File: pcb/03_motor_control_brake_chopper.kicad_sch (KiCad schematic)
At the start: 0 parts

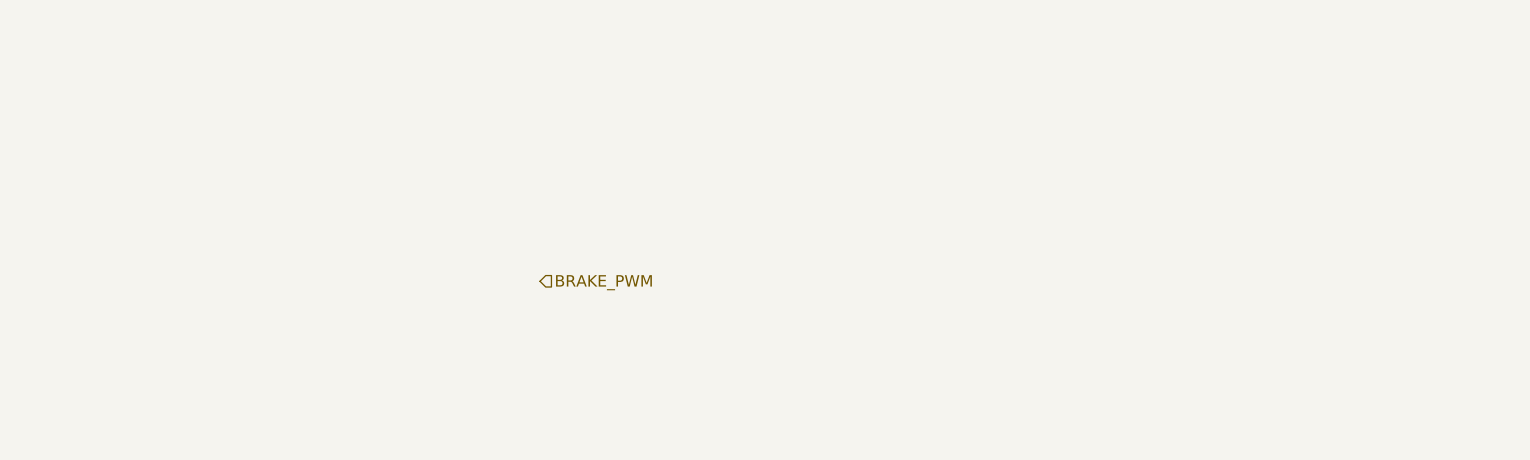
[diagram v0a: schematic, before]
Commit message: Implemented brake chopper control with low side mosfet
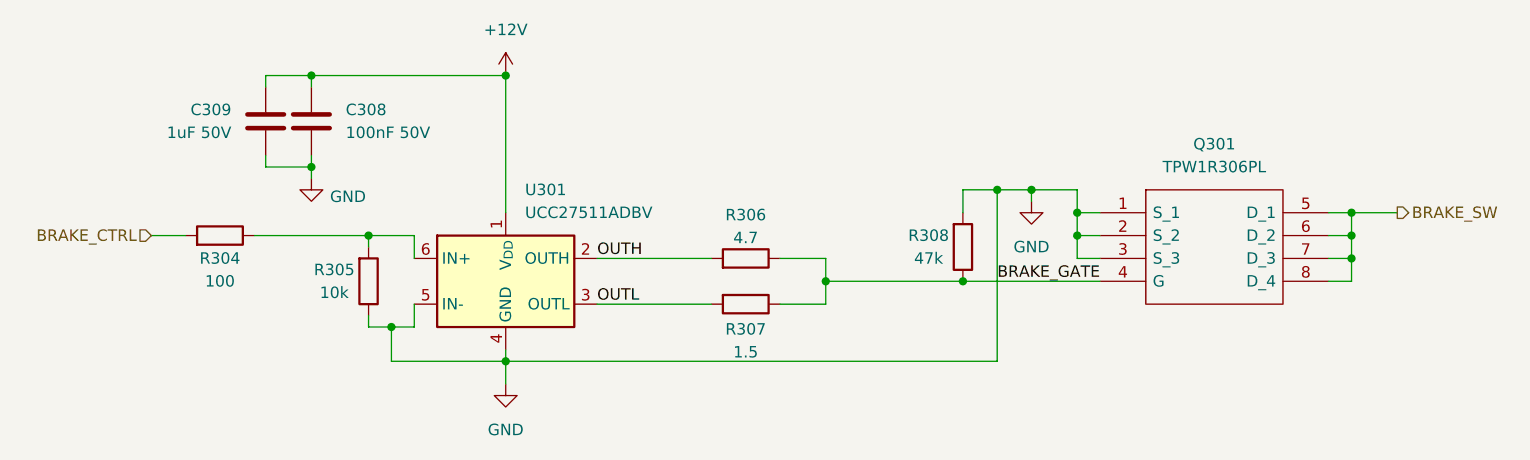
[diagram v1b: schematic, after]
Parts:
- added C308: 100nF 50V, FluxNode-FOC:C_0402_1005_DensityHigh, symbol Device:C
- added C309: 1uF 50V, FluxNode-FOC:C_0603_1608_DensityHigh, symbol Device:C
- added Q301: TPW1R306PL, FluxNode-FOC:SOP_ADVANCE, symbol FluxNode-FOC:TPW1R306PL
- added R304: 100, FluxNode-FOC:R_0402_1005_DensityHigh, symbol Device:R
- added R305: 10k, FluxNode-FOC:R_0402_1005_DensityHigh, symbol Device:R
- added R306: 4.7, FluxNode-FOC:R_0603_1608_DensityHigh, symbol Device:R
- added R307: 1.5, FluxNode-FOC:R_0603_1608_DensityHigh, symbol Device:R
- added R308: 47k, FluxNode-FOC:R_0402_1005_DensityHigh, symbol Device:R
- added U301: UCC27511ADBV, Package_TO_SOT_SMD:SOT-23-6, symbol Driver_FET:UCC27511ADBV
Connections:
- new net: R304.1, R305.2, U301.6 (IN+)
- new net +12V: C308.1, C309.1, U301.1 (V_{DD})
- new net BRAKE_CTRL: R304.2
- new net BRAKE_GATE: Q301.4 (G), R306.1, R307.1, R308.1
- new net BRAKE_SW: Q301.5 (D_1), Q301.6 (D_2), Q301.7 (D_3), Q301.8 (D_4)
- new net GND: C308.2, C309.2, Q301.1 (S_1), Q301.2 (S_2), Q301.3 (S_3), R305.1, R308.2, U301.4 (GND), U301.5 (IN-)
- new net OUTH: R306.2, U301.2 (OUTH)
- new net OUTL: R307.2, U301.3 (OUTL)

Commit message: Unified all different LCSC part numbers of the same exact components to just one variant
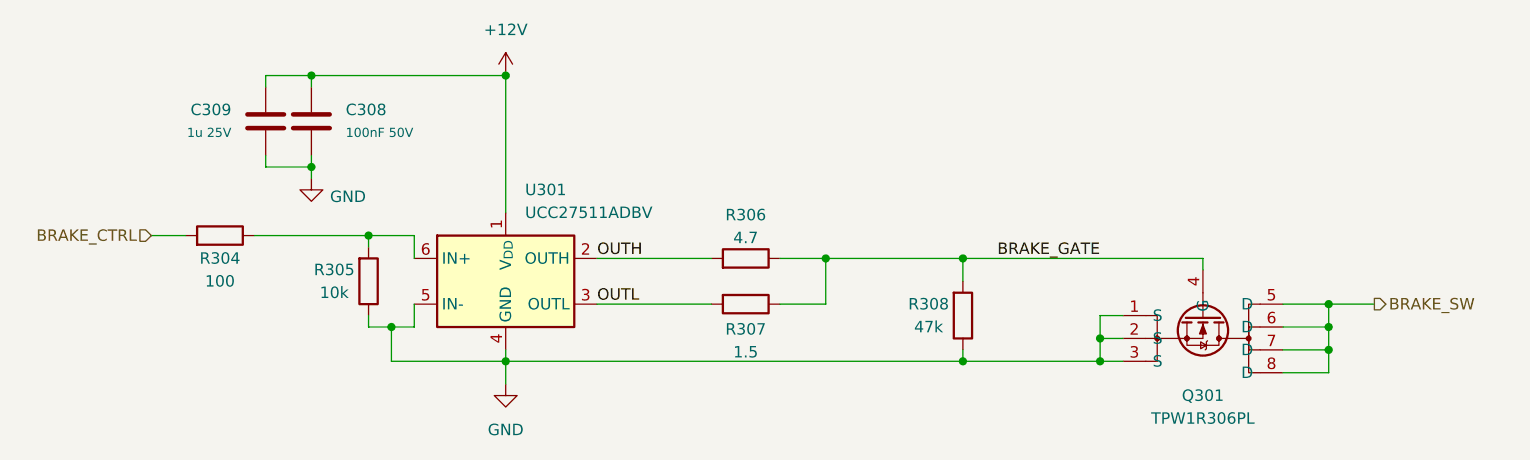
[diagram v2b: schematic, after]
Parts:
- C308: LCSC (none) -> C361198; MPN (none) -> C1005X7R1H104KT000F
- C309: value 1uF 50V -> 1u 25V; LCSC (none) -> C386079; MPN (none) -> TMK107AB7105KAHT
- R304: LCSC (none) -> C705627; MPN (none) -> RT0402BRD07100RL
- R306: LCSC (none) -> C54921054; MPN (none) -> HRC0603J4R7 ENTN
- R307: LCSC (none) -> C2906978; MPN (none) -> FRC0603F1R50TS
- R308: LCSC (none) -> C144757; MPN (none) -> AC0402FR-0747KL
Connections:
- net BRAKE_GATE: now also R308.2; no longer R308.1
- net GND: now also R308.1; no longer R308.2
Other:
- company: (none) -> PhiMai
- moved on the sheet: R308
